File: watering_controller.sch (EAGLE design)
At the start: 9 parts, among them IC2 7805T, J1 DCJ0202, Q1 IRF510

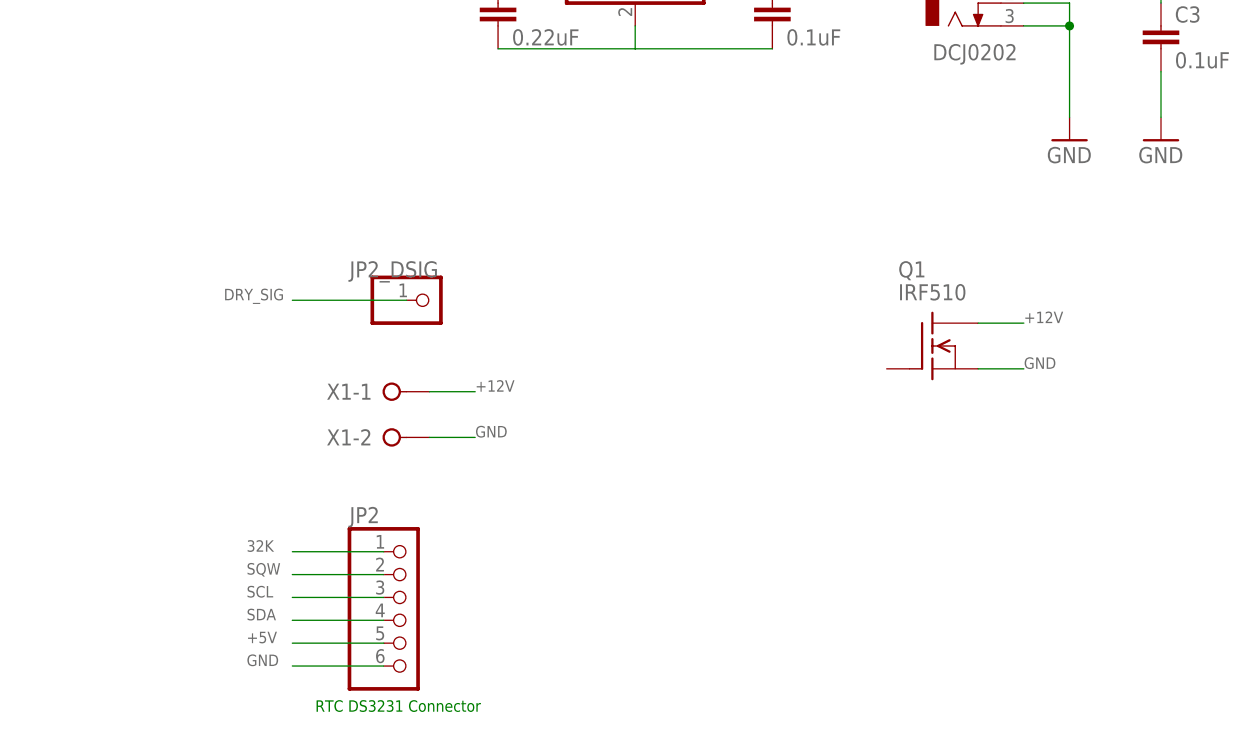
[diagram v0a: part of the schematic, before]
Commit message: Add pull-down resistor for MOSFET and changed MOSFET type to IRLZ44N
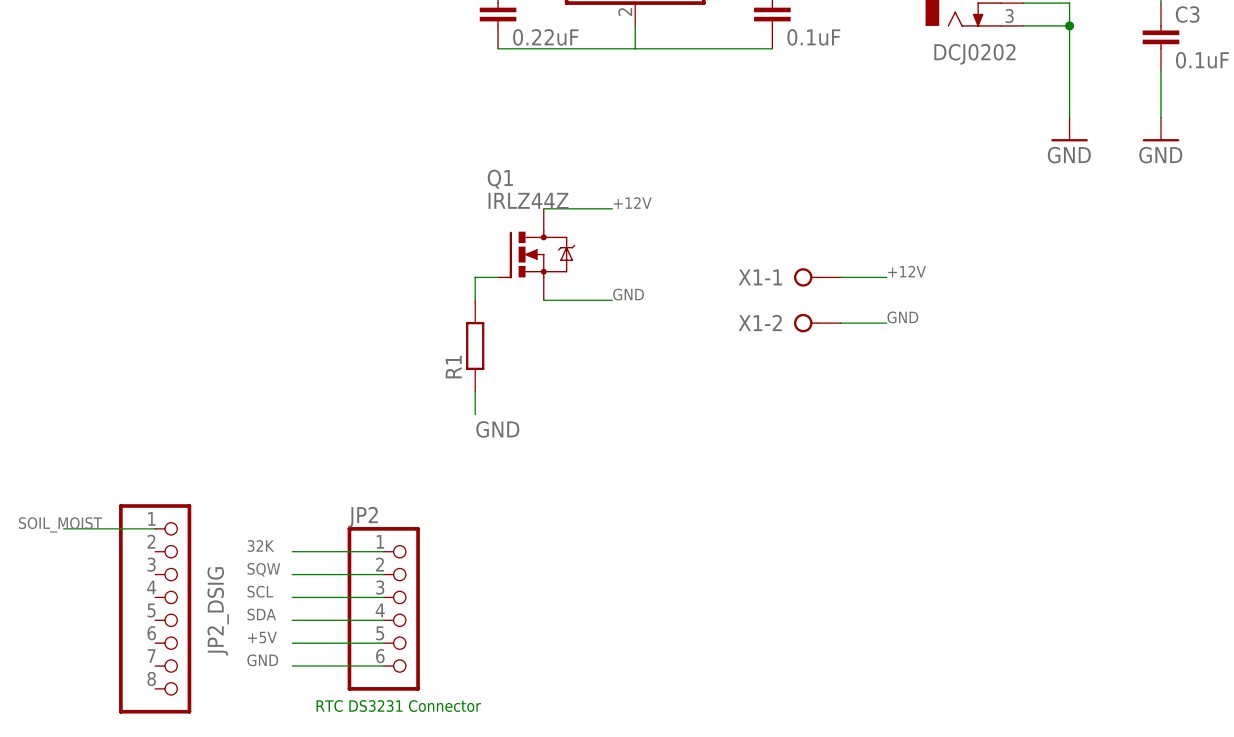
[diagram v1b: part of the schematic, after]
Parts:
- added R1: (no value), resistor:R-EU_0204/5
- JP1: device pinhead:PINHD-1X1 -> pinhead:PINHD-1X8
- Q1: value IRF510 -> IRLZ44Z; device transistor-fet:IRF510 -> transistor-power:IRLZ44Z
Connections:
- net DRY_SIG renamed SOIL_MOIST
- new net N$1: Q1.G, R1.2
- net GND: now also R1.1
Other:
- moved on the sheet: X1-1, X1-2
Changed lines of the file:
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@@
 <grid distance="0.1" unitdist="inch" unit="inch" style="lines" multiple="1" display="no" altdistance="0.01" altunitdist="inch" altunit="inch"/>
 <layers>
-<layer number="1" name="Top" color="4" fill="1" visible="no" active="no"/>
-<layer number="16" name="Bottom" color="1" fill="1" visible="no" active="no"/>
-<layer number="17" name="Pads" color="2" fill="1" visible="no" active="no"/>
-<layer number="18" name="Vias" color="2" fill="1" visible="no" active="no"/>
-<layer number="19" name="Unrouted" color="6" fill="1" visible="no" active="no"/>
-<layer number="20" name="Dimension" color="15" fill="1" visible="no" active="no"/>
-<layer number="21" name="tPlace" color="7" fill="1" visible="no" active="no"/>
-<layer number="22" name="bPlace" color="7" fill="1" visible="no" active="no"/>
-<layer number="23" name="tOrigins" color="15" fill="1" visible="no" active="no"/>
-<layer number="24" name="bOrigins" color="15" fill="1" visible="no" active="no"/>
-<layer number="25" name="tNames" color="7" fill="1" visible="no" active="no"/>
-<layer number="26" name="bNames" color="7" fill="1" visible="no" active="no"/>
-<layer number="27" name="tValues" color="7" fill="1" visible="no" active="no"/>
-<layer number="28" name="bValues" color="7" fill="1" visible="no" active="no"/>
+<layer number="1" name="Top" color="4" fill="1" visible="yes" active="no"/>
+<layer number="16" name="Bottom" color="1" fill="1" visible="yes" active="no"/>
+<layer number="17" name="Pads" color="2" fill="1" visible="yes" active="no"/>
+<layer number="18" name="Vias" color="2" fill="1" visible="yes" active="no"/>
+<layer number="19" name="Unrouted" color="6" fill="1" visible="yes" active="no"/>
+<layer number="20" name="Dimension" color="15" fill="1" visible="yes" active="no"/>
+<layer number="21" name="tPlace" color="7" fill="1" visible="yes" active="no"/>
+<layer number="22" name="bPlace" color="7" fill="1" visible="yes" active="no"/>
+<layer number="23" name="tOrigins" color="15" fill="1" visible="yes" active="no"/>
+<layer number="24" name="bOrigins" color="15" fill="1" visible="yes" active="no"/>
+<layer number="25" name="tNames" color="7" fill="1" visible="yes" active="no"/>
+<layer number="26" name="bNames" color="7" fill="1" visible="yes" active="no"/>
+<layer number="27" name="tValues" color="7" fill="1" visible="yes" active="no"/>
+<layer number="28" name="bValues" color="7" fill="1" visible="yes" active="no"/>
 <layer number="29" name="tStop" color="7" fill="3" visible="no" active="no"/>
 <layer number="30" name="bStop" color="7" fill="6" visible="no" active="no"/>
@@
 <layer number="35" name="tGlue" color="7" fill="4" visible="no" active="no"/>
 <layer number="36" name="bGlue" color="7" fill="5" visible="no" active="no"/>
-<layer number="37" name="tTest" color="7" fill="1" visible="no" active="no"/>
-<layer number="38" name="bTest" color="7" fill="1" visible="no" active="no"/>
+<layer number="37" name="tTest" color="7" fill="1" visible="yes" active="no"/>
+<layer number="38" name="bTest" color="7" fill="1" visible="yes" active="no"/>
 <layer number="39" name="tKeepout" color="4" fill="11" visible="no" active="no"/>
 <layer number="40" name="bKeepout" color="1" fill="11" visible="no" active="no"/>
@@
 <layer number="44" name="Drills" color="7" fill="1" visible="no" active="no"/>
 <layer number="45" name="Holes" color="7" fill="1" visible="no" active="no"/>
-<layer number="46" name="Milling" color="3" fill="1" visible="no" active="no"/>
-<layer number="47" name="Measures" color="7" fill="1" visible="no" active="no"/>
-<layer number="48" name="Document" color="7" fill="1" visible="no" active="no"/>
-<layer number="49" name="Reference" color="7" fill="1" visible="no" active="no"/>
-<layer number="51" name="tDocu" color="7" fill="1" visible="no" active="no"/>
-<layer number="52" name="bDocu" color="7" fill="1" visible="no" active="no"/>
+<layer number="46" name="Milling" color="3" fill="1" visible="yes" active="no"/>
+<layer number="47" name="Measures" color="7" fill="1" visible="yes" active="no"/>
+<layer number="48" name="Document" color="7" fill="1" visible="yes" active="no"/>
+<layer number="49" name="Reference" color="7" fill="1" visible="yes" active="no"/>
+<layer number="51" name="tDocu" color="7" fill="1" visible="yes" active="no"/>
+<layer number="52" name="bDocu" color="7" fill="1" visible="yes" active="no"/>
 <layer number="90" name="Modules" color="5" fill="1" visible="yes" active="yes"/>
 <layer number="91" name="Nets" color="2" fill="1" visible="yes" active="yes"/>
@@
 <part name="C4" library="rcl" deviceset="C-EU" device="025-025X050" value="0.22uF"/>
 <part name="C5" library="rcl" deviceset="C-EU" device="025-025X050" value="0.1uF"/>
-<part name="JP1" library="pinhead" deviceset="PINHD-1X1" device="" value="JP2_DSIG"/>
+<part name="JP1" library="pinhead" deviceset="PINHD-1X8" device="" value="JP2_DSIG"/>
 <part name="X1" library="con-wago-508" deviceset="W237-02P" device=""/>
-<part name="Q1" library="transistor-fet" deviceset="IRF510" device=""/>
+<part name="Q1" library="transistor-power" deviceset="IRLZ44Z" device=""/>
 <part name="JP2" library="pinhead" deviceset="PINHD-1X6" device=""/>
+<part name="R1" library="resistor" deviceset="R-EU_" device="0204/5"/>
 </parts>
 <sheets>
@@
 <instance part="C4" gate="G$1" x="10.16" y="116.84"/>
 <instance part="C5" gate="G$1" x="40.64" y="116.84"/>
-<instance part="JP1" gate="G$1" x="2.54" y="83.82" smashed="yes">
-<attribute name="VALUE" x="-6.35" y="86.36" size="1.778" layer="96"/>
+<instance part="JP1" gate="A" x="-25.4" y="48.26" smashed="yes">
+<attribute name="VALUE" x="-20.32" y="44.45" size="1.778" layer="96" rot="R90"/>
 </instance>
-<instance part="X1" gate="-1" x="-2.54" y="73.66"/>
-<instance part="X1" gate="-2" x="-2.54" y="68.58"/>
-<instance part="Q1" gate="G$1" x="58.42" y="78.74" smashed="yes">
-<attribute name="VALUE" x="54.61" y="83.82" size="1.778" layer="96"/>
-<attribute name="NAME" x="54.61" y="86.36" size="1.778" layer="95"/>
+<instance part="X1" gate="-1" x="43.18" y="86.36"/>
+<instance part="X1" gate="-2" x="43.18" y="81.28"/>
+<instance part="Q1" gate="G$1" x="12.7" y="88.9" smashed="yes">
+<attribute name="VALUE" x="8.89" y="93.98" size="1.778" layer="96"/>
+<attribute name="NAME" x="8.89" y="96.52" size="1.778" layer="95"/>
 </instance>
 <instance part="JP2" gate="A" x="0" y="48.26"/>
+<instance part="R1" gate="G$1" x="7.62" y="78.74" rot="R90"/>
 </instances>
 <busses>
@@
 <segment>
 <pinref part="X1" gate="-2" pin="KL"/>
-<wire x1="2.54" y1="68.58" x2="7.62" y2="68.58" width="0.1524" layer="91"/>
-<label x="7.62" y="68.58" size="1.27" layer="95"/>
+<wire x1="48.26" y1="81.28" x2="53.34" y2="81.28" width="0.1524" layer="91"/>
+<label x="53.34" y="81.28" size="1.27" layer="95"/>
 </segment>
 <segment>
 <pinref part="Q1" gate="G$1" pin="S"/>
-<wire x1="63.5" y1="76.2" x2="68.58" y2="76.2" width="0.1524" layer="91"/>
-<label x="68.58" y="76.2" size="1.27" layer="95"/>
+<wire x1="15.24" y1="83.82" x2="22.86" y2="83.82" width="0.1524" layer="91"/>
+<label x="22.86" y="83.82" size="1.27" layer="95"/>
 </segment>
 <segment>
@@
 <wire x1="-2.54" y1="43.18" x2="-12.7" y2="43.18" width="0.1524" layer="91"/>
 <label x="-17.78" y="43.18" size="1.27" layer="95"/>
+</segment>
+<segment>
+<pinref part="R1" gate="G$1" pin="1"/>
+<wire x1="7.62" y1="73.66" x2="7.62" y2="71.12" width="0.1524" layer="91"/>
+<label x="7.62" y="68.58" size="1.778" layer="95"/>
 </segment>
 </net>
@@
 <segment>
 <pinref part="X1" gate="-1" pin="KL"/>
-<wire x1="2.54" y1="73.66" x2="7.62" y2="73.66" width="0.1524" layer="91"/>
-<label x="7.62" y="73.66" size="1.27" layer="95"/>
+<wire x1="48.26" y1="86.36" x2="53.34" y2="86.36" width="0.1524" layer="91"/>
+<label x="53.34" y="86.36" size="1.27" layer="95"/>
 </segment>
 <segment>
 <pinref part="Q1" gate="G$1" pin="D"/>
-<wire x1="63.5" y1="81.28" x2="68.58" y2="81.28" width="0.1524" layer="91"/>
-<label x="68.58" y="81.28" size="1.27" layer="95"/>
-</segment>
-</net>
-<net name="DRY_SIG" class="0">
-<segment>
-<pinref part="JP1" gate="G$1" pin="1"/>
-<wire x1="0" y1="83.82" x2="-12.7" y2="83.82" width="0.1524" layer="91"/>
-<label x="-20.32" y="83.82" size="1.27" layer="95"/>
+<wire x1="15.24" y1="93.98" x2="22.86" y2="93.98" width="0.1524" layer="91"/>
+<label x="22.86" y="93.98" size="1.27" layer="95"/>
+</segment>
+</net>
+<net name="SOIL_MOIST" class="0">
+<segment>
+<pinref part="JP1" gate="A" pin="1"/>
+<wire x1="-27.94" y1="58.42" x2="-38.1" y2="58.42" width="0.1524" layer="91"/>
+<label x="-43.18" y="58.42" size="1.27" layer="95"/>
 </segment>
 </net>
@@
 </segment>
 </net>
+<net name="N$1" class="0">
+<segment>
+<pinref part="Q1" gate="G$1" pin="G"/>
+<pinref part="R1" gate="G$1" pin="2"/>
+<wire x1="10.16" y1="86.36" x2="7.62" y2="86.36" width="0.1524" layer="91"/>
+<wire x1="7.62" y1="86.36" x2="7.62" y2="83.82" width="0.1524" layer="91"/>
+</segment>
+</net>

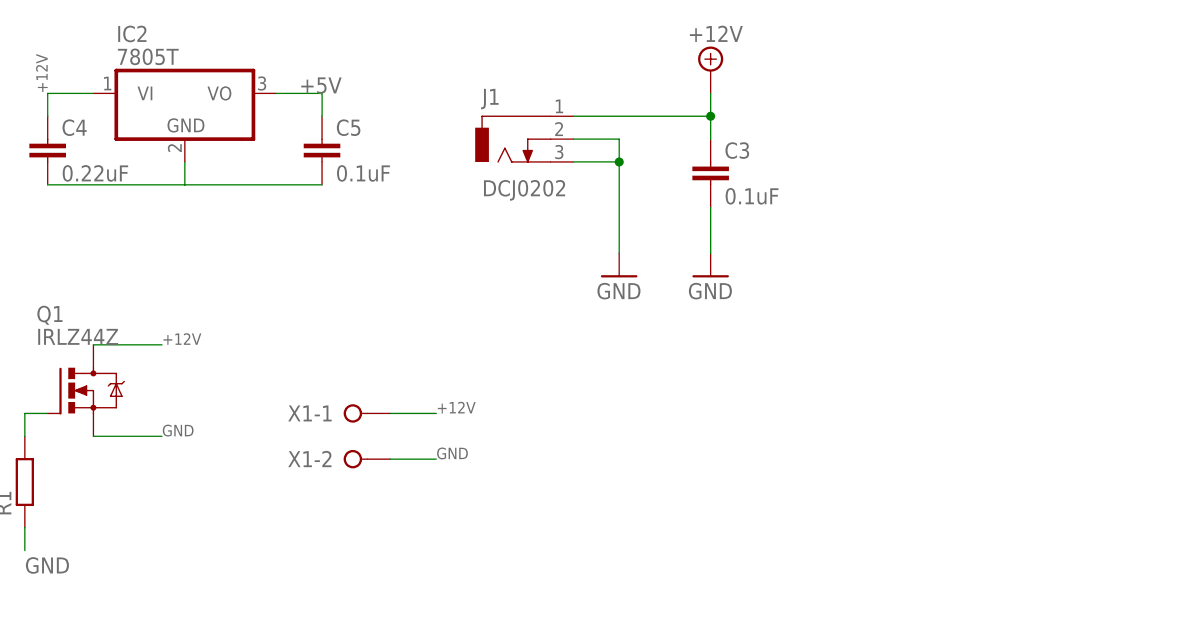
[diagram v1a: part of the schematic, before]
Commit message: Update drill files for production
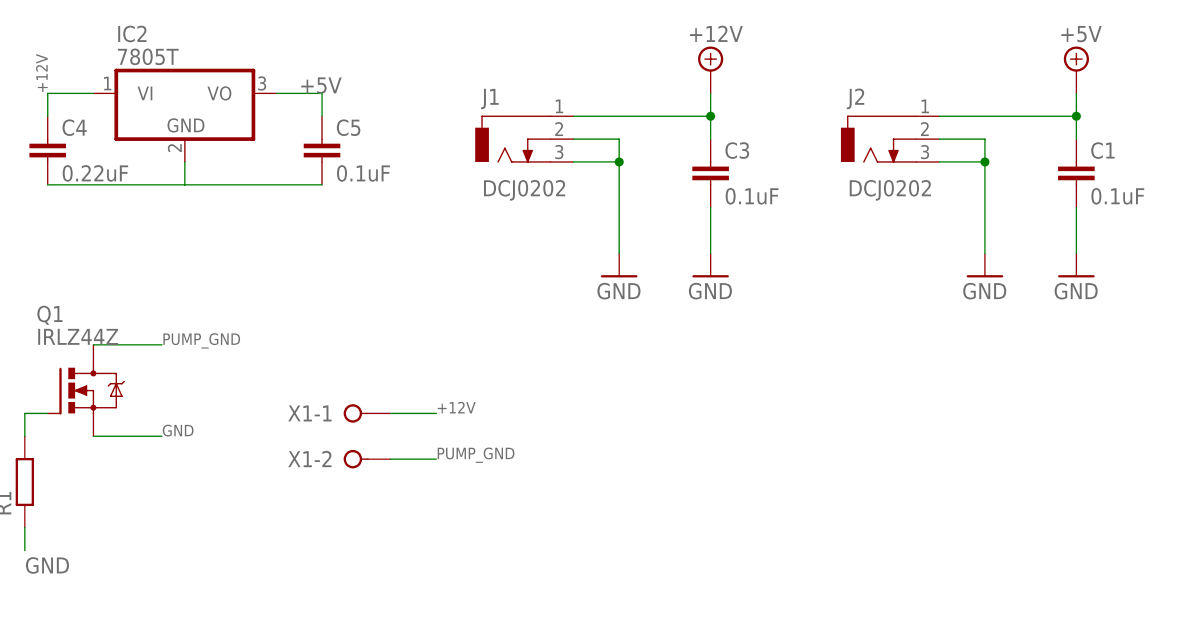
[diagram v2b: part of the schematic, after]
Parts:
- added C1: 0.1uF, rcl:C-EU025-025X050
- added J2: DCJ0202, con-jack:DCJ0202
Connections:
- new net PUMP_GND: Q1.D, X1-2.KL
- net +12V: no longer Q1.D
- net +9V: now also C1.1, J2.1
- net GND: now also C1.2, J2.2, J2.3; no longer X1-2.KL
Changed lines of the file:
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@@
 <part name="JP2" library="pinhead" deviceset="PINHD-1X6" device=""/>
 <part name="R1" library="resistor" deviceset="R-EU_" device="0204/5"/>
+<part name="P+2" library="supply2" deviceset="+5V" device=""/>
+<part name="GND3" library="supply1" deviceset="GND" device=""/>
+<part name="J2" library="con-jack" deviceset="DCJ0202" device=""/>
+<part name="GND4" library="supply1" deviceset="GND" device=""/>
+<part name="C1" library="rcl" deviceset="C-EU" device="025-025X050" value="0.1uF"/>
 </parts>
 <sheets>
@@
 <instance part="JP2" gate="A" x="0" y="48.26"/>
 <instance part="R1" gate="G$1" x="7.62" y="78.74" rot="R90"/>
+<instance part="P+2" gate="+5V" x="124.46" y="124.46"/>
+<instance part="GND3" gate="1" x="124.46" y="101.6"/>
+<instance part="J2" gate="G$1" x="101.6" y="116.84"/>
+<instance part="GND4" gate="1" x="114.3" y="101.6"/>
+<instance part="C1" gate="G$1" x="124.46" y="114.3"/>
 </instances>
 <busses>
@@
 <junction x="83.82" y="119.38"/>
 <pinref part="C3" gate="G$1" pin="1"/>
+</segment>
+<segment>
+<pinref part="J2" gate="G$1" pin="1"/>
+<pinref part="P+2" gate="+5V" pin="+5V"/>
+<wire x1="109.22" y1="119.38" x2="124.46" y2="119.38" width="0.1524" layer="91"/>
+<wire x1="124.46" y1="119.38" x2="124.46" y2="121.92" width="0.1524" layer="91"/>
+<wire x1="124.46" y1="119.38" x2="124.46" y2="116.84" width="0.1524" layer="91"/>
+<junction x="124.46" y="119.38"/>
+<pinref part="C1" gate="G$1" pin="1"/>
 </segment>
 </net>
@@
 </segment>
 <segment>
-<pinref part="X1" gate="-2" pin="KL"/>
-<wire x1="48.26" y1="81.28" x2="53.34" y2="81.28" width="0.1524" layer="91"/>
-<label x="53.34" y="81.28" size="1.27" layer="95"/>
-</segment>
-<segment>
 <pinref part="Q1" gate="G$1" pin="S"/>
 <wire x1="15.24" y1="83.82" x2="22.86" y2="83.82" width="0.1524" layer="91"/>
@@
 <wire x1="7.62" y1="73.66" x2="7.62" y2="71.12" width="0.1524" layer="91"/>
 <label x="7.62" y="68.58" size="1.778" layer="95"/>
+</segment>
+<segment>
+<pinref part="GND3" gate="1" pin="GND"/>
+<wire x1="124.46" y1="104.14" x2="124.46" y2="109.22" width="0.1524" layer="91"/>
+<pinref part="C1" gate="G$1" pin="2"/>
+</segment>
+<segment>
+<pinref part="J2" gate="G$1" pin="2"/>
+<wire x1="109.22" y1="116.84" x2="114.3" y2="116.84" width="0.1524" layer="91"/>
+<pinref part="GND4" gate="1" pin="GND"/>
+<wire x1="114.3" y1="116.84" x2="114.3" y2="114.3" width="0.1524" layer="91"/>
+<pinref part="J2" gate="G$1" pin="3"/>
+<wire x1="114.3" y1="114.3" x2="114.3" y2="104.14" width="0.1524" layer="91"/>
+<wire x1="109.22" y1="114.3" x2="114.3" y2="114.3" width="0.1524" layer="91"/>
+<junction x="114.3" y="114.3"/>
 </segment>
 </net>
@@
 <label x="53.34" y="86.36" size="1.27" layer="95"/>
 </segment>
-<segment>
-<pinref part="Q1" gate="G$1" pin="D"/>
-<wire x1="15.24" y1="93.98" x2="22.86" y2="93.98" width="0.1524" layer="91"/>
-<label x="22.86" y="93.98" size="1.27" layer="95"/>
-</segment>
 </net>
 <net name="SOIL_MOIST" class="0">
@@
 </segment>
 </net>
+<net name="PUMP_GND" class="0">
+<segment>
+<pinref part="X1" gate="-2" pin="KL"/>
+<wire x1="48.26" y1="81.28" x2="53.34" y2="81.28" width="0.1524" layer="91"/>
+<label x="53.34" y="81.28" size="1.27" layer="95"/>
+</segment>
+<segment>
+<pinref part="Q1" gate="G$1" pin="D"/>
+<wire x1="15.24" y1="93.98" x2="22.86" y2="93.98" width="0.1524" layer="91"/>
+<label x="22.86" y="93.98" size="1.27" layer="95"/>
+</segment>
+</net>
